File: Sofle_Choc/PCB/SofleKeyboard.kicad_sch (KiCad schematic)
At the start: 84 parts, among them J2 4PIN, J3 OLED, P1 i2c_pin, P2 i2c_pin, SW1 SW_PUSH_LED, SW10 SW_PUSH_LED, SW11 SW_PUSH_LED, SW12 SW_PUSH_LED, SW13 SW_PUSH_LED, SW14 SW_PUSH_LED, SW15 SW_PUSH_LED, SW16 SW_PUSH_LED, SW17 SW_PUSH_LED, SW18 SW_PUSH_LED, SW19 SW_PUSH_LED, SW2 SW_PUSH_LED, SW20 SW_PUSH_LED, SW21 SW_PUSH_LED, SW22 SW_PUSH_LED, SW23 SW_PUSH_LED, SW24 SW_PUSH_LED, SW25 Rotary_Encoder_Switch, SW26 SW_PUSH_LED, SW27 SW_PUSH_LED, SW28 SW_PUSH_LED, SW29 SW_PUSH_LED, SW3 SW_PUSH_LED, SW30 SW_PUSH_LED, SW4 SW_PUSH_LED, SW5 SW_PUSH_LED, SW6 SW_PUSH_LED, SW7 SW_PUSH_LED, SW8 SW_PUSH_LED, SW9 SW_PUSH_LED, U1 ProMicro

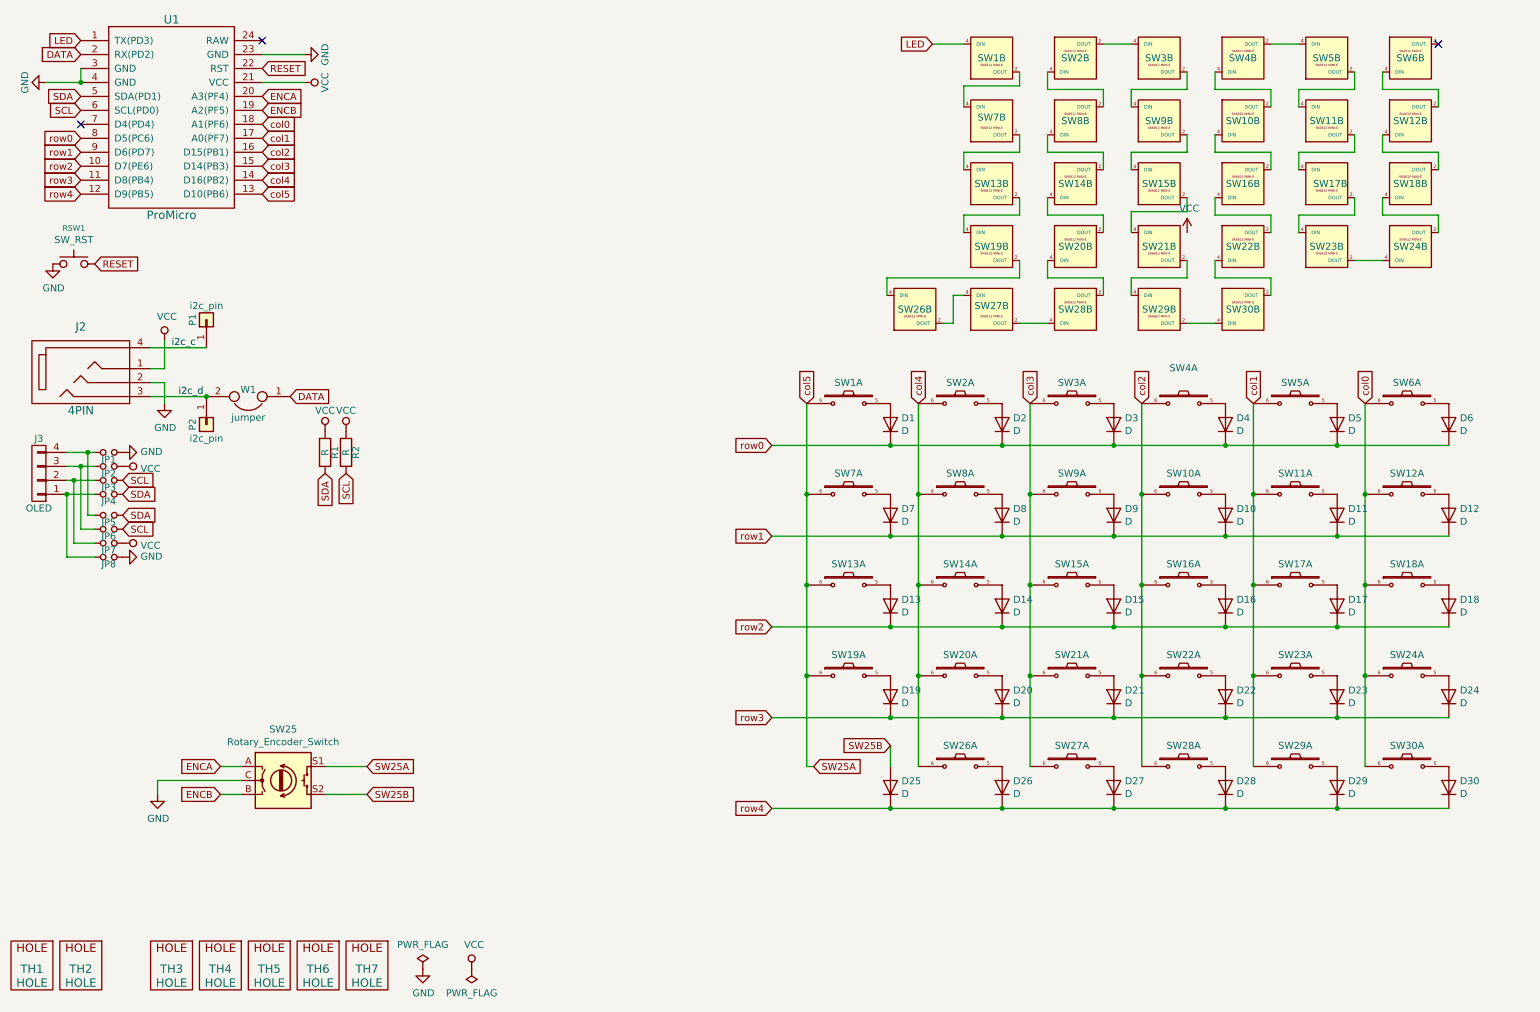
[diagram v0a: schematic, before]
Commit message: Add 7th row and move thumb cluster
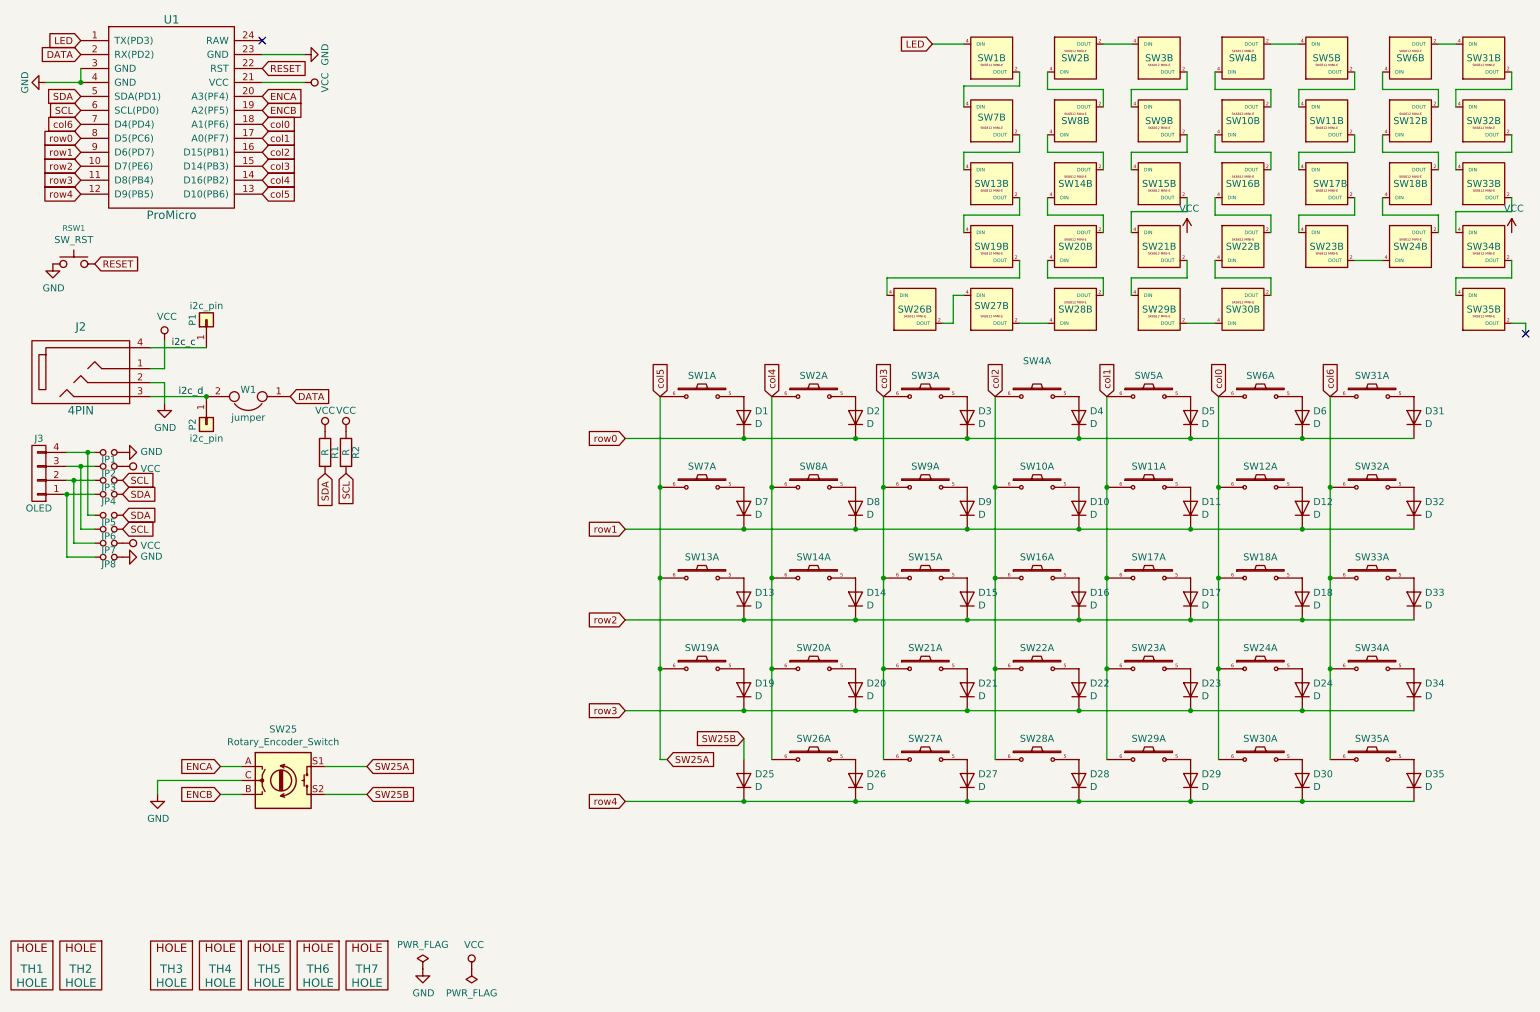
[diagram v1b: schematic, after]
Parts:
- added D31, D32, D33, D34, D35: D, SofleKeyboard-footprint:Diode_SOD123, symbol SofleKeyboard-rescue:D-Lily58-cache-Lily58_Pro-rescue
- added SW31, SW32, SW33, SW34, SW35: SW_PUSH_LED, SofleChoc:Choc_Hotswap_SK6812MiniE, symbol SofleKeyboard:SW_PUSH_LED
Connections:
- net GND: now also SW31.3 (GND), SW32.3 (GND), SW33.3 (GND), SW34.3 (GND), SW35.3 (GND)
- net VCC: now also SW31.1 (VDD), SW32.1 (VDD), SW33.1 (VDD), SW34.1 (VDD), SW35.1 (VDD)
- net row0: now also D31.1 (K)
- net row1: now also D32.1 (K)
- net row2: now also D33.1 (K)
- net row3: now also D34.1 (K)
- net row4: now also D35.1 (K)
- net col6: now reaches U1.7 (D4(PD4))
- net col6: now also SW31.6, SW32.6, SW33.6, SW34.6, SW35.6
- net at SW6.2 (DOUT): now also SW31.4 (DIN)
- new net: D35.2 (A), SW35.5
- new net: SW34.2 (DOUT), SW35.4 (DIN)
- new net: SW33.2 (DOUT), SW34.4 (DIN)
- new net: D34.2 (A), SW34.5
- new net: SW31.2 (DOUT), SW32.4 (DIN)
- new net: D33.2 (A), SW33.5
- new net: D31.2 (A), SW31.5
- new net: SW32.2 (DOUT), SW33.4 (DIN)
- new net: D32.2 (A), SW32.5
- no-connect marks 3 -> 2
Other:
- moved on the sheet: D1, D10, D11, D12, D13, D14, D15, D16, D17, D18, D19, D2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
